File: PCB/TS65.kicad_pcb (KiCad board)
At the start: 2 copper layers, 299.5 x 105.8 mm, 437 parts, among them P1 USB_CONN, P11 2PIN, P12 2PIN, P13 2PIN, P15 2PIN, P2 USB3, P3 USB3_MICRO, P4 6PIN, P5 6PIN, P6 ISP6, P7_1 5PIN, P7_2 5PIN, U1 Atmega32u4, U2 MCP23018, U3 IP4234CZ6, U4 74HC138, U5 PAM2804, X1 CRYSTAL

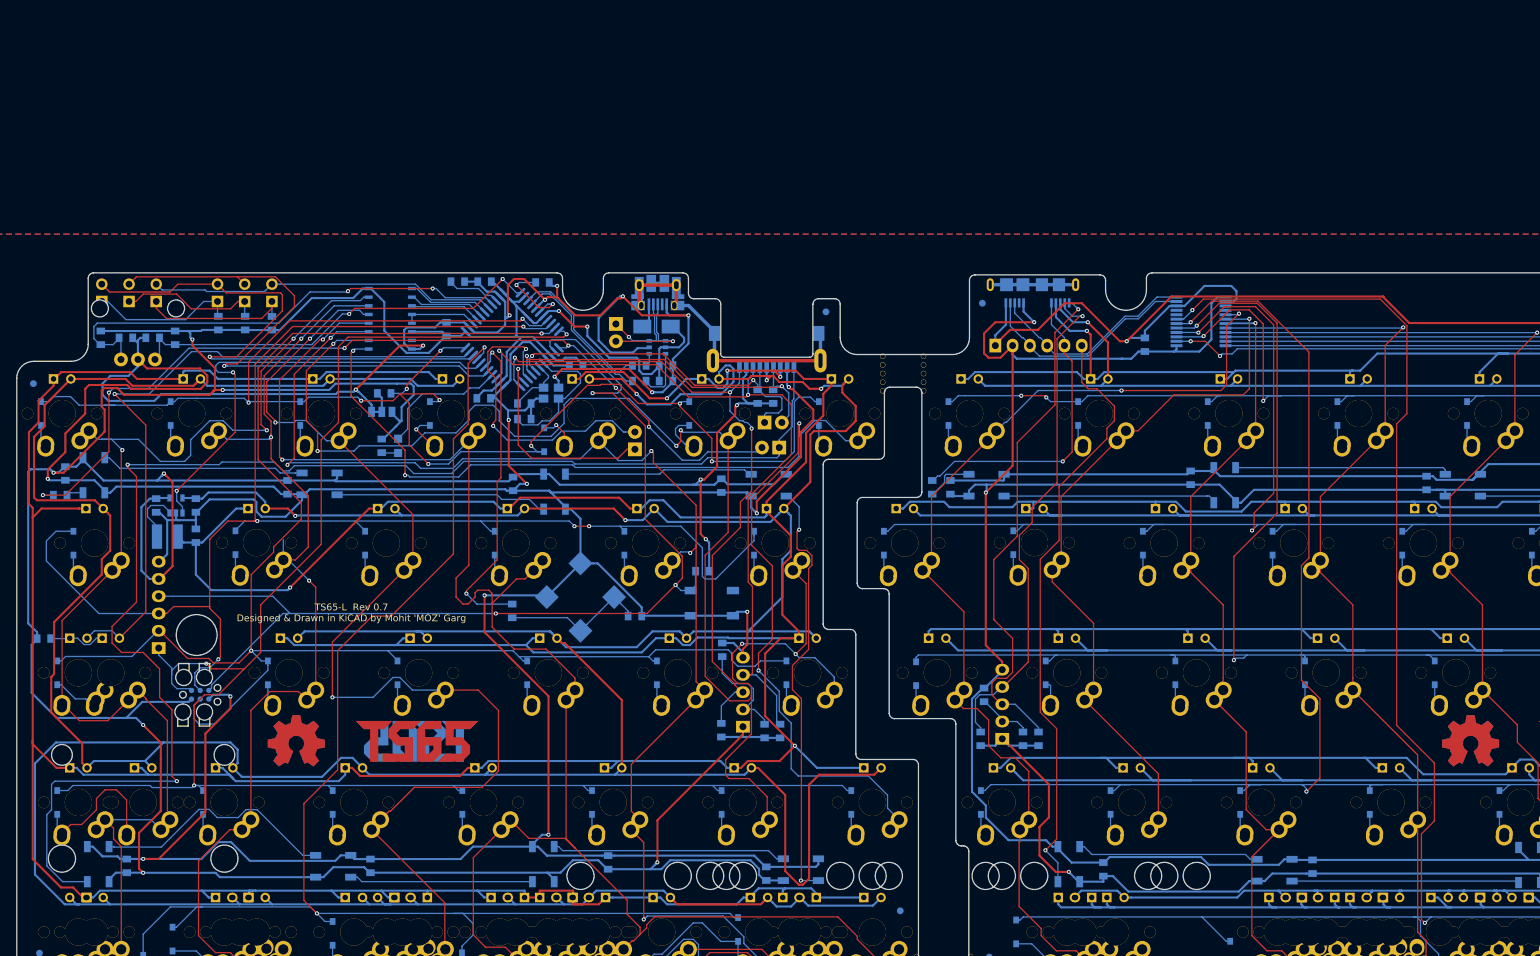
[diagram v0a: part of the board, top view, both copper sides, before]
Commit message: Updating schematic to use STM32F303CC microcontroller instead of ATMEGA32U4; next steps: swapping out USB3 interconnect for HDMI.
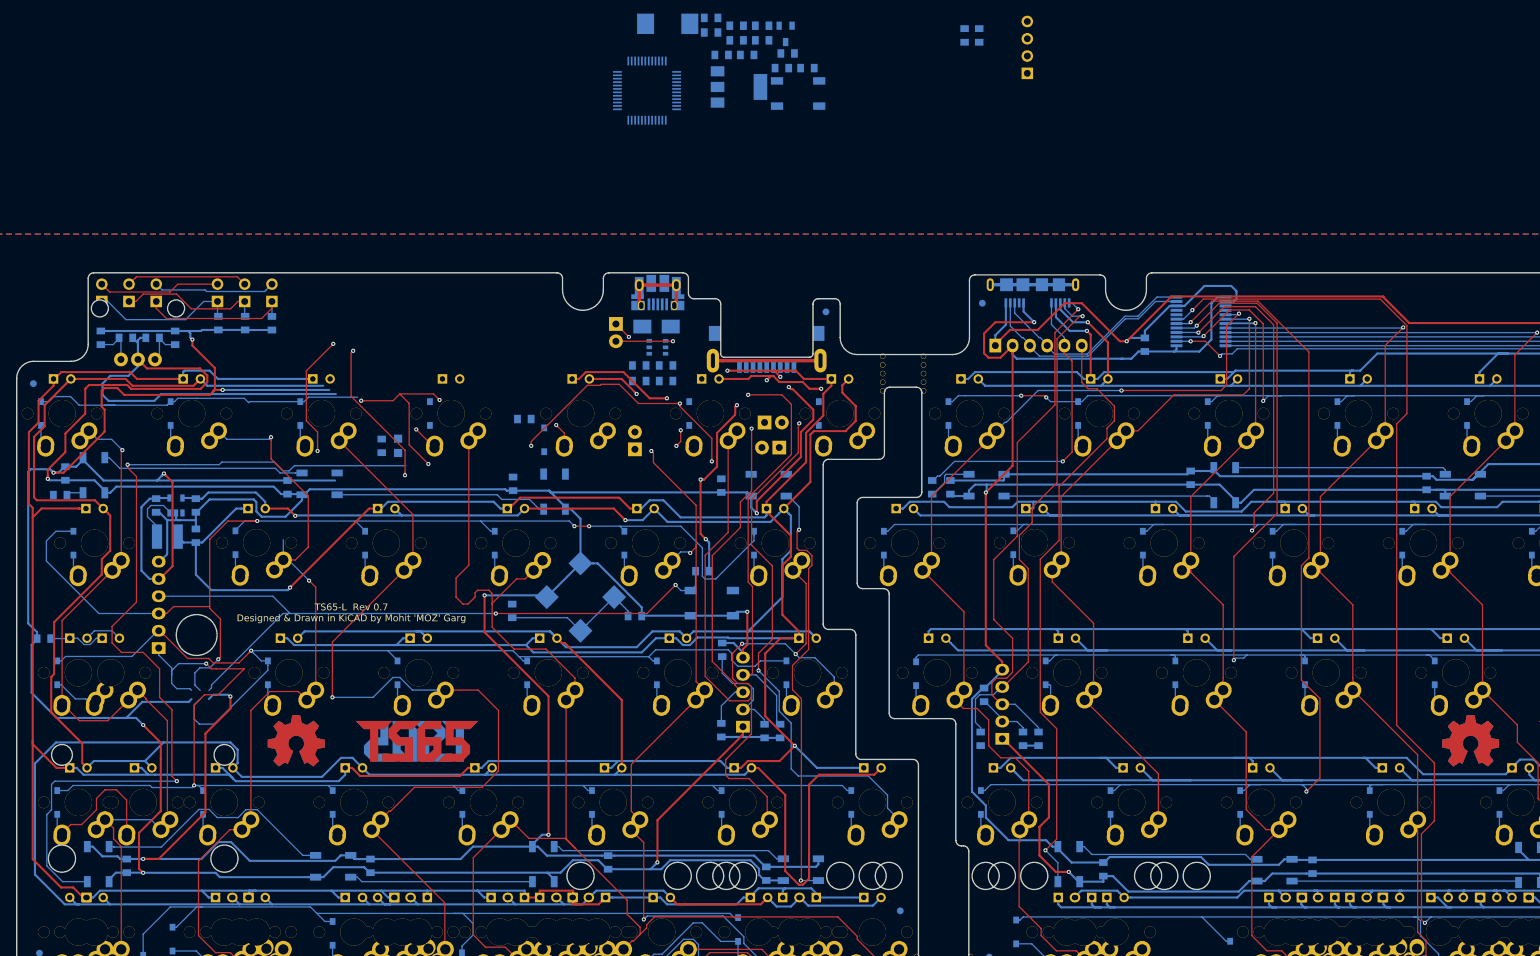
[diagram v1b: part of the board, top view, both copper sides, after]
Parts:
- removed C14: 8pF, prettylib:SMD_0805
- removed JP1: JUMPER, prettylib:JUMPER_SMD_3
- removed P6: ISP6, prettylib:TC2030_BIG
- removed U1: Atmega32u4, prettylib:TQFP44
- removed U4: 74HC138, prettylib:SO-16-N
- removed X1: CRYSTAL, prettylib:NX3225SA
- added J1: Programming, Connector_PinHeader_2.54mm:PinHeader_1x04_P2.54mm_Vertical, B.Cu at (230.0, 38.5)
- added Q1: NTR1P02T1G - PMOS, prettylib:SOT-23, B.Cu at (194.5, 32.7)
- added R1: 1.5k, prettylib:SMD_0805, B.Cu at (187.3, 31.5)
- added R2: 10k, prettylib:SMD_0805, B.Cu at (191.0, 33.6)
- added R7: 100k, prettylib:SMD_0805, B.Cu at (194.8, 35.6)
- added R8: 10k, prettylib:SMD_0805, B.Cu at (222.9, 32.9)
- added S3: TAC_SWITCH, prettylib:TACT_5.2x5.2, B.Cu at (196.3, 41.4)
- added U6: AP1117-33, Package_TO_SOT_SMD:SOT-223-3_TabPin2, B.Cu at (187.6, 40.5)
- added U7: STM32F303CCTx, Package_QFP:LQFP-48_7x7mm_P0.5mm, B.Cu at (174.1, 41.0)
- added Y1: 8M ABM2-8.000MHZ-D4Y-T, prettylib:ABRACON-ABM2_xtal, B.Cu at (177.2, 31.2)
- C13: value 8pF -> 22pF
- C2: value 1uF -> 22uF
- C3: value 0.1uF -> 22pF
- moved R9 100.2 mm to (220.8, 32.9), turned to 90 degrees
- moved C4 65.4 mm to (193.9, 37.7)
- moved C7 60.2 mm to (187.3, 33.6), turned to 0 degrees
- moved R6 54.5 mm to (191.0, 31.5), turned to 0 degrees
- moved C5 54.0 mm to (188.8, 35.8)
- moved C9 51.1 mm to (183.5, 30.3), turned to 0 degrees
- moved C3 50.4 mm to (185.1, 35.8), turned to 0 degrees
- moved R5 48.5 mm to (197.7, 37.7), turned to 0 degrees
- moved C2 44.3 mm to (183.5, 32.5)
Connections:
- C2 pad 1: Net-(C2-Pad1) -> +3V3
- C3 pad 1: +5V -> /mcu/XTAL1
- C4 pad 1: +5V -> VSS
- C4 pad 2: VSS -> +3V3
- C5 pad 1: Net-(C5-Pad1) -> VSS
- C5 pad 2: VSS -> +3V3
- C6 pad 1: +5V -> +3V3
- C7 pad 1: +5V -> VSS
- C7 pad 2: VSS -> +3V3
- C9 pad 1: +5V -> VSS
- C9 pad 2: VSS -> +3V3
- P1 pad 4: Net-(P1-Pad4) -> (no net)
- P2 pad 1: +5V -> +3V3
- P3 pad 1: +5V -> +3V3
- P3 pad 4: Net-(P3-Pad4) -> (no net)
- P4 pad 1: /RowL4 -> (no net)
- P4 pad 2: /RowL3 -> (no net)
- P4 pad 3: /RowL2 -> (no net)
- P5 pad 1: +5V -> +3V3
- R14 pad 2: +5V -> +3V3
- R5 pad 1: +5V -> +3V3
- R6 pad 1: +5V -> +3V3
- R71 pad 2: +5V -> +3V3
- R72 pad 1: +5V -> +3V3
- R9 pad 1: VSS -> /mcu/SWDIO
- R9 pad 2: /mcu/HWBE -> VSS
- S1 pad 1: Net-(S1-Pad1) -> (no net)
- U2 pad 10: +5V -> +3V3
- U2 pad 14: +5V -> +3V3
- U2 pad 15: Net-(U2-Pad15) -> (no net)
- U2 pad 16: Net-(U2-Pad16) -> (no net)
- U2 pad 8: Net-(U2-Pad8) -> (no net)
- U2 pad 9: Net-(U2-Pad9) -> (no net)
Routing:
- net +5V: track 1276.4 -> 970.3 mm, vias 16 -> 10
- net VSS: track 1174.6 -> 974.0 mm, vias 21 -> 10
- net /ledmatrix/RGBLDIN: track 131.8 -> 0.00 mm, vias 6 -> 0
- net /RowL1: track 213.1 -> 111.8 mm, vias 8 -> 6
- net /RowL5: track 208.5 -> 109.7 mm, vias 2 -> 0
- net /ledmatrix/LEDCL: track 100.4 -> 5.67 mm, vias 1 -> 0
- net /RowL3: track 235.2 -> 141.9 mm, vias 2 -> 1
- net /RowL4: track 256.5 -> 167.9 mm, vias 3 -> 2
- net /Col5: track 215.5 -> 128.9 mm, vias 5 -> 3
- net /Col6: track 217.9 -> 139.1 mm
- net /Col7: track 181.2 -> 103.5 mm
- net /ledmatrix/RGBLDOUT: track 204.7 -> 134.0 mm
- net /RowL2: track 230.6 -> 161.2 mm, vias 5 -> 4
- net /mcu/LEDBL: track 67.8 -> 0.00 mm, vias 2 -> 0
- net /ledmatrix/LEDI1: track 83.0 -> 18.0 mm, vias 1 -> 0
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
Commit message: Updating design to use STM32F303 instead of AVR32u4.
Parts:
- removed BREAKHOLES5, BREAKHOLES6: MISC, prettylib:BreakHoles
- removed P11, P12, P13, P15: 2PIN, prettylib:Pin_Header_1x02
- removed P2: USB3, prettylib:USB3_AFEMALE_MOD
- removed P3: USB3_MICRO, prettylib:USB3_MICROB
- removed P4, P5: 6PIN, prettylib:Pin_Header_1x06
- added J2: INTERCONNECT, prettylib:47151-0001, B.Cu at (233.3, 78.4)
- added J3: INTERCONNECT, prettylib:47151-0001, B.Cu at (190.5, 78.3)
- added J4: UART, Connector_PinHeader_2.54mm:PinHeader_1x03_P2.54mm_Vertical, F.Cu at (116.5, 85.6)
- added J5: I2C, Connector_PinHeader_2.54mm:PinHeader_1x04_P2.54mm_Vertical, F.Cu at (193.0, 85.8)
- added J6: JOYSTICK, Connector_PinHeader_2.54mm:PinHeader_1x04_P2.54mm_Vertical, F.Cu at (155.0, 87.3)
- added Q2: NDS332P, prettylib:SOT-23, B.Cu at (101.5, 98.1)
- C2: footprint prettylib:SMD_0805 -> Resistor_SMD:R_1206_3216Metric
- moved J1 114.2 mm to (122.7, 77.6)
- moved R9 107.6 mm to (124.5, 80.8), turned to 0 degrees
- moved R8 107.4 mm to (125.2, 77.6), turned to 270 degrees
- moved S3 89.2 mm to (116.2, 80.6)
- moved R7 75.9 mm to (126.7, 69.1), turned to 180 degrees
- moved C7 71.8 mm to (129.0, 75.6), turned to 90 degrees
- moved C5 70.1 mm to (136.5, 82.3), turned to 180 degrees
- moved C9 64.4 mm to (132.0, 68.8)
- moved R2 62.1 mm to (174.0, 93.3), turned to 180 degrees
- moved Q1 60.5 mm to (173.9, 89.5)
- moved C4 59.9 mm to (146.2, 73.8), turned to 180 degrees
- moved R1 56.4 mm to (173.0, 86.1)
- moved U7 51.3 mm to (136.0, 75.3), turned to 225 degrees
- moved R6 50.5 mm to (168.7, 76.8), turned to 90 degrees
- moved S1 49.5 mm to (150.5, 79.6), turned to 90 degrees
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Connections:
- LEDG20 pad 2: /ledmatrix/RGBRDOUT -> (no net)
- R24 pad 2: /ledmatrix/RGBLDIN -> Net-(Q2-Pad3)
- U7 pad 10: /mcu/TPCLK -> /ledmatrix/LEDCL
- U7 pad 11: /mcu/TPDATA -> /mcu/JOY_X
- U7 pad 12: /mcu/BUZZER -> /mcu/JOY_Y
- U7 pad 13: /mcu/USB_RESET -> /Col7
- U7 pad 14: /ledmatrix/LEDI3 -> /Col6
- U7 pad 15: /ledmatrix/LEDCL -> /Col5
- U7 pad 16: /ledmatrix/LEDI1 -> /Col4
- U7 pad 17: /ledmatrix/LEDI2 -> /Col3
- U7 pad 18: /Col4 -> /Col2
- U7 pad 19: /Col5 -> /Col1
- U7 pad 2: /Col1 -> /ledmatrix/LEDI3
- U7 pad 20: /Col6 -> /ledmatrix/LEDI4
- U7 pad 21: /RowL1 -> /mcu/USB_RESET
- U7 pad 22: /RowL2 -> /mcu/BUZZER
- U7 pad 25: /RowL3 -> /RowL5
- U7 pad 27: /mcu/LEDBL -> /RowL3
- U7 pad 28: /ledmatrix/RGBLDIN -> /RowL2
- U7 pad 29: /ledmatrix/LEDI4 -> /RowL1
- U7 pad 3: /Col2 -> /ledmatrix/LEDI2
- U7 pad 38: (no net) -> /mcu/TPCLK
- U7 pad 39: /Col7 -> /mcu/TPDATA
- U7 pad 4: /Col3 -> /ledmatrix/LEDI1
- U7 pad 40: /mcu/ENCB -> /mcu/ENCA
- U7 pad 41: /mcu/ENCA -> /mcu/ENCB
- U7 pad 45: /ledmatrix/RGBLDIN -> /mcu/LEDBL
- U7 pad 46: /RowL5 -> /ledmatrix/RGBLDIN
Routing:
- net +3V3: track 57.7 -> 275.1 mm, vias 4 -> 11
- net VSS: track 974.0 -> 821.2 mm, vias 10 -> 24
- net (no net): track 0.00 -> 97.1 mm, vias 0 -> 2
- net /RowL5: track 109.7 -> 204.3 mm, vias 0 -> 2
- net /mcu/SCL: track 0.00 -> 88.6 mm, vias 0 -> 5
- net /ledmatrix/RGBRDOUT: track 88.5 -> 0.00 mm, vias 1 -> 0
- net /mcu/TPCLK: track 49.7 -> 137.9 mm, vias 1 -> 4
- net /mcu/SDA: track 0.00 -> 88.2 mm, vias 0 -> 5
- net /mcu/MCURST: track 101.3 -> 21.1 mm
- net /ledmatrix/LEDCL: track 5.67 -> 84.6 mm, vias 0 -> 1
- net /mcu/TPDATA: track 61.5 -> 137.5 mm, vias 1 -> 4
- net /ledmatrix/LEDCATH: track 728.2 -> 799.6 mm, vias 5 -> 3
- net /mcu/LEDBL: track 0.00 -> 56.6 mm, vias 0 -> 2
- net /Col1: track 123.0 -> 178.9 mm, vias 1 -> 4
- net /ledmatrix/RGBLDIN: track 0.00 -> 55.7 mm, vias 0 -> 2
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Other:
- board size 299.5 x 105.8 mm -> 299.5 x 105.9 mm
- board text added: "TS65-STM32F3-L Rev 1.0 Designed & Drawn in KiCAD by Mohit 'MOZ' Garg and Adam Coddington"
- board text added: "TS65-STM32F3-R Rev 1.0 Designed & Drawn in KiCAD by Mohit 'MOZ' Garg and Adam Coddington"
- board text removed: "TS65-L Rev 0.7 Designed & Drawn in KiCAD by Mohit 'MOZ' Garg"
- board text removed: "TS65-R Rev 0.7 Designed & Drawn in KiCAD by Mohit 'MOZ' Garg"
